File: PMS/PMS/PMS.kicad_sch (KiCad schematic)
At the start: 22 parts

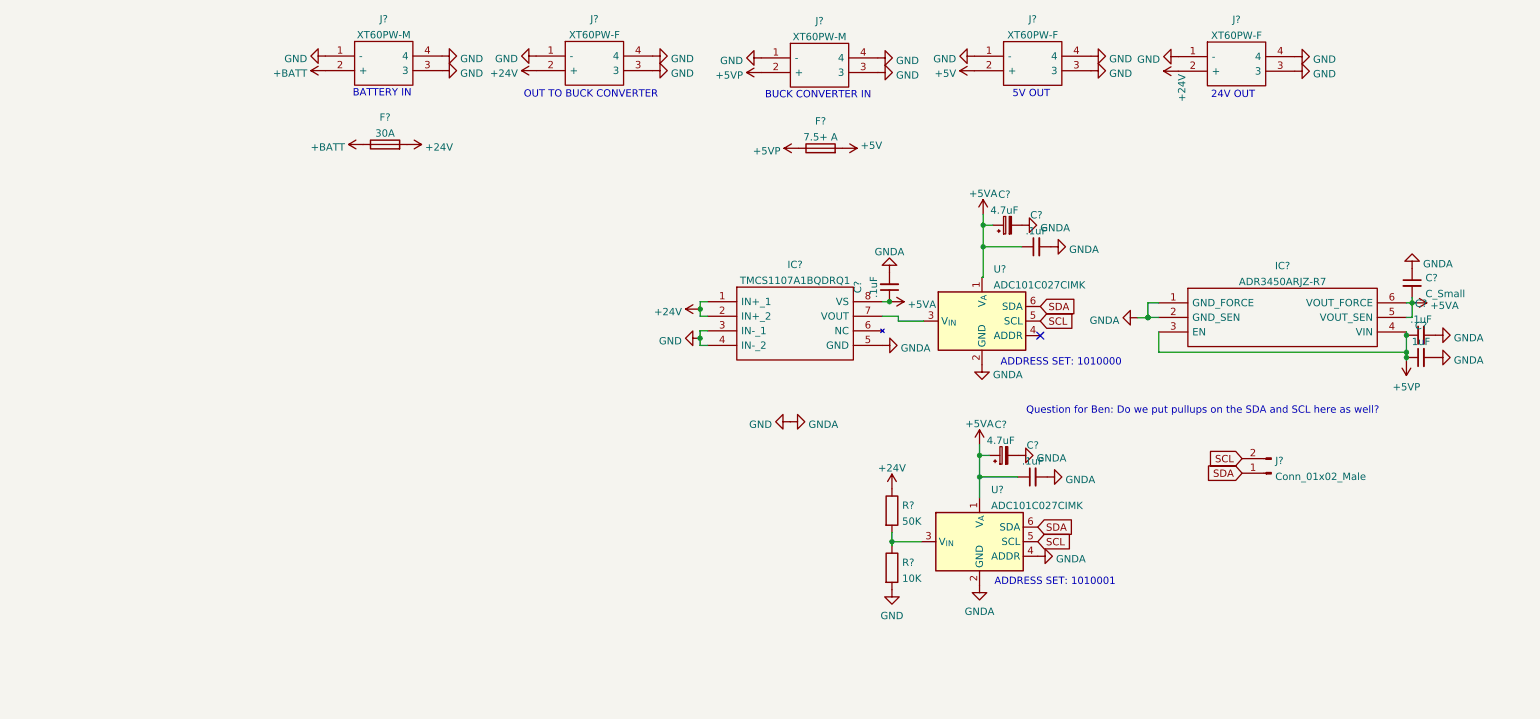
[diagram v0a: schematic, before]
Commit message: several changes to satisfy ERC
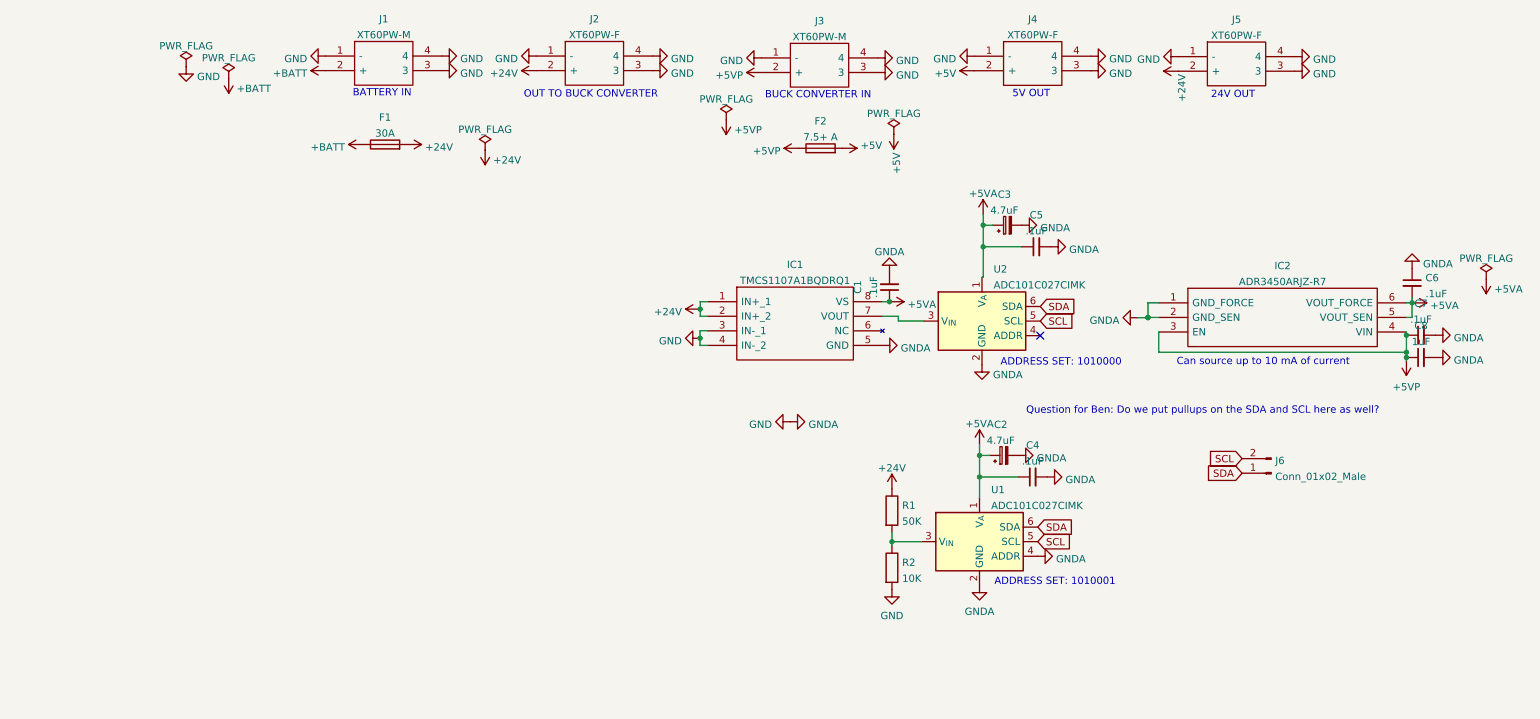
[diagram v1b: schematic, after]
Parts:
- C6: renamed from C?; value C_Small -> .1uF
- IC1: renamed from IC?; footprint SOIC127P600X175-8N -> TMCS1107A1BQDRQ1:SOIC127P600X175-8N
- IC2: renamed from IC?; footprint SOT95P280X145-6N -> ADR3450ARJZ-R7:SOT95P280X145-6N
- J1, J3: renamed from J?; footprint XT60PWM -> LIB_XT60PW-M:XT60PWM
- J2, J4, J5: renamed from J?; footprint XT60PWM -> LIB_XT60PW-F:XT60PWF
- J6: renamed from J?; footprint (none) -> Connector_Molex:Molex_KK-254_AE-6410-02A_1x02_P2.54mm_Vertical
- gave numbers to parts that had none: 13
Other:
- note added: "Can source up to 10 mA of current"

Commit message: Updated PMS. Now includes option for LA12 with other fixes.
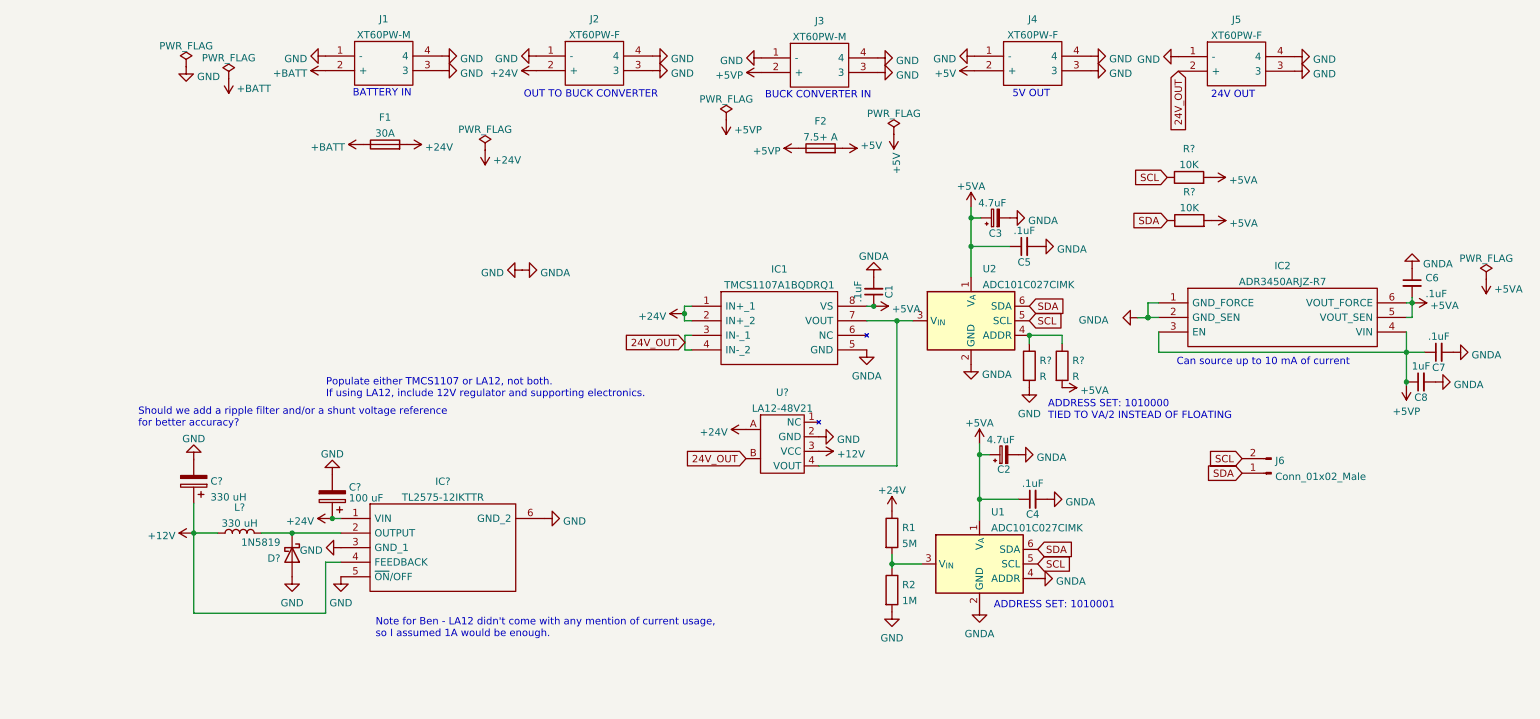
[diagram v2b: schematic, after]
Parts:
- added C?: 330 uH, symbol Device:C_Polarized
- added C?: 100 uF, symbol Device:C_Polarized
- added D?: 1N5819, Diode_THT:D_DO-41_SOD81_P10.16mm_Horizontal, symbol Diode:1N5819
- added IC?: TL2575-12IKTTR, Package_TO_SOT_SMD:TO-263-5_TabPin6, symbol TL2575-12IKTTR:TL2575-12IKTTR
- added L?: 330 uH, symbol Device:L
- added R? (x2): 10K, symbol Device:R
- added R? (x2): R, symbol Device:R
- added U?: LA12-48V21, LA12:LA12-48V21, symbol LA12:LA12-48V21
- R1: value 50K -> 5M
- R2: value 10K -> 1M
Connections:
- net +24V: now also C?.1, IC?.1 (VIN), U?.A; no longer J5.2 (+)
- net +5VA: now also R?.2, R?.2, R?.2
- net GND: now also C?.2, C?.2, D?.2 (A), IC?.3 (GND_1), IC?.5 (~{ON}/OFF), IC?.6 (GND_2), R?.2, U?.2 (GND); no longer IC1.3 (IN-_1), IC1.4 (IN-_2)
- net SCL: now also R?.1
- net SDA: now also R?.1
- net at IC1.7 (VOUT), U2.3 (V_{IN}): now also U?.4 (VOUT)
- net at U2.4 (ADDR): now also R?.1, R?.1
- new net: D?.1 (K), IC?.2 (OUTPUT), L?.2
- new net +12V: C?.1, IC?.4 (FEEDBACK), L?.1, U?.3 (VCC)
- new net 24V_OUT: IC1.3 (IN-_1), IC1.4 (IN-_2), J5.2 (+), U?.B
- no-connect marks 1 -> 0
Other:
- note added: "ADDRESS SET: 1010000 TIED TO VA/2 INSTEAD OF FLOATING"
- note added: "Note for Ben - LA12 didn't come with any mention of current usage, so I assumed 1A would be enough."
- note added: "Populate either TMCS1107 or LA12, not both. If using LA12, include 12V regulator and supporting electronics."
- note added: "Should we add a ripple filter and/or a shunt voltage reference for better accuracy?"
- note removed: "ADDRESS SET: 1010000"
- note removed: "Question for Ben: Do we put pullups on the SDA and SCL here as well?"
- moved on the sheet: C1, C3, C4, C5, C7, C8, IC1, R1, R2, U1, U2

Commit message: annotated schematic
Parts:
- R3, R4: renamed from R?; value R -> 10K
- gave numbers to parts that had none: 8
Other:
- moved on the sheet: R4

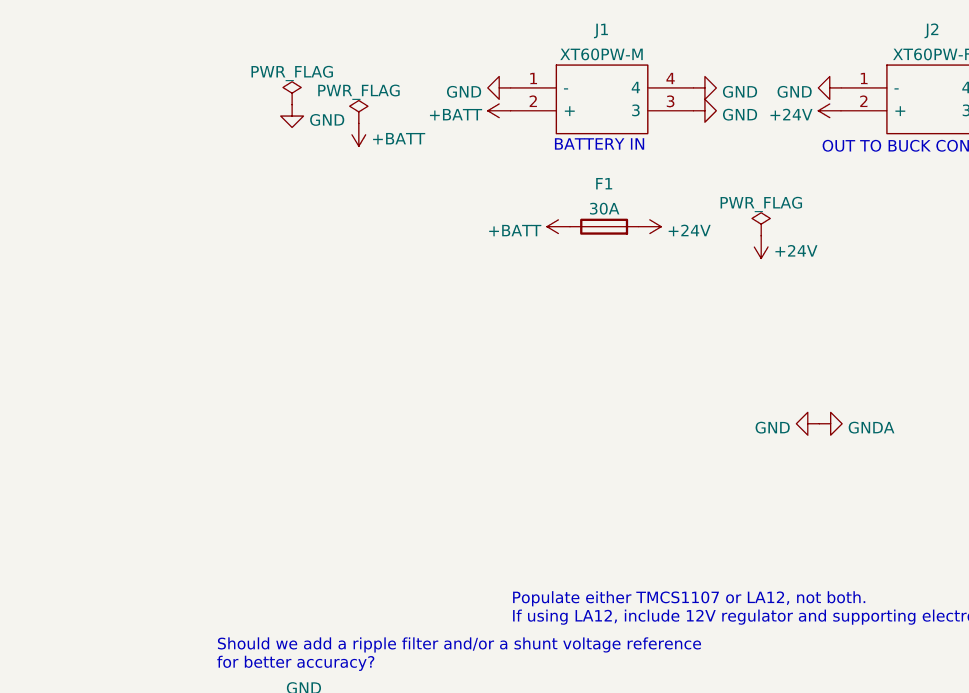
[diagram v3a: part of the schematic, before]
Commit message: added reverse polarity protection
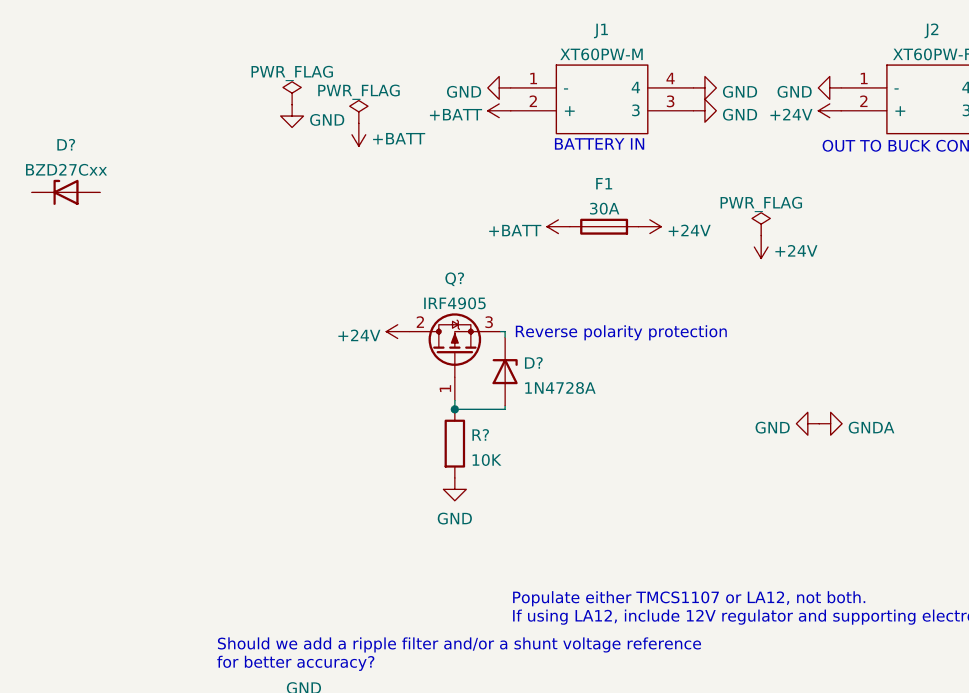
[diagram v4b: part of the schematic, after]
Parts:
- added D?: 1N4728A, Diode_THT:D_DO-41_SOD81_P10.16mm_Horizontal, symbol Diode:1N47xxA
- added D?: BZD27Cxx, Diode_SMD:D_SMF, symbol Diode:BZD27Cxx
- added Q?: IRF4905, Package_TO_SOT_THT:TO-220-3_Vertical, symbol Transistor_FET:IRF4905
- added R?: 10K, symbol Device:R
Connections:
- net +24V: now also Q?.2 (D)
- net GND: now also R?.2
- new net: D?.2 (A), Q?.1 (G), R?.1
- new net: D?.1 (K), Q?.3 (S)
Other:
- note added: "Reverse polarity protection"
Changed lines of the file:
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@@
   (junction (at 242.1128 75.2602) (diameter 0) (color 0 0 0 0)
   )
+  (junction (at 46.482 67.945) (diameter 0) (color 0 0 0 0)
+  )
   (wire (pts (xy 196.0626 77.8002) (xy 196.0626 77.851))
     (stroke (width 0) (type default) (color 0 0 0 0))
@@
     (stroke (width 0) (type default) (color 0 0 0 0))
   )
+  (wire (pts (xy 46.482 67.945) (xy 52.07 67.945))
+    (stroke (width 0) (type default) (color 0 0 0 0))
+  )
   (wire (pts (xy 242.1128 75.2602) (xy 242.1128 77.8002))
     (stroke (width 0) (type default) (color 0 0 0 0))
@@
     (stroke (width 0) (type default) (color 0 0 0 0))
   )
+  (wire (pts (xy 52.07 59.309) (xy 51.562 59.309))
+    (stroke (width 0) (type default) (color 0 0 0 0))
+  )
+  (wire (pts (xy 52.07 67.945) (xy 52.07 67.564))
+    (stroke (width 0) (type default) (color 0 0 0 0))
+  )
   (wire (pts (xy 166.7002 109.4994) (xy 173.4312 109.4994))
     (stroke (width 0) (type default) (color 0 0 0 0))
@@
     (stroke (width 0) (type default) (color 0 0 0 0))
   )
+  (wire (pts (xy 46.482 66.929) (xy 46.482 67.945))
+    (stroke (width 0) (type default) (color 0 0 0 0))
+  )
   (wire (pts (xy 152.2984 78.3844) (xy 155.067 78.3844))
     (stroke (width 0) (type default) (color 0 0 0 0))
@@
   )
   (wire (pts (xy 197.9422 83.8708) (xy 241.1222 83.8708))
+    (stroke (width 0) (type default) (color 0 0 0 0))
+  )
+  (wire (pts (xy 52.07 59.944) (xy 52.07 59.309))
     (stroke (width 0) (type default) (color 0 0 0 0))
   )
@@
   )
   (text "24V OUT" (at 207.0608 39.7764 0)
+    (effects (font (size 1.27 1.27)) (justify left bottom))
+  )
+  (text "Reverse polarity protection" (at 53.086 60.325 0)
     (effects (font (size 1.27 1.27)) (justify left bottom))
   )
@@
     (pin "1")
   )
+  (symbol (lib_id "Device:R") (at 46.482 71.755 0) (unit 1)
+    (in_bom yes) (on_board yes) (fields_autoplaced)
+    (property "Reference" "R?" (id 0) (at 48.26 70.8465 0)
+      (effects (font (size 1.27 1.27)) (justify left))
+    )
+    (property "Value" "10K" (id 1) (at 48.26 73.6216 0)
+      (effects (font (size 1.27 1.27)) (justify left))
+    )
+    (property "Footprint" "" (id 2) (at 44.704 71.755 90)
+      (effects (font (size 1.27 1.27)) hide)
+    )
+    (property "Datasheet" "~" (id 3) (at 46.482 71.755 0)
+      (effects (font (size 1.27 1.27)) hide)
+    )
+    (pin "1")
+    (pin "2")
+  )
   (symbol (lib_id "power:GNDA") (at 173.482 101.727 90) (unit 1)
     (in_bom yes) (on_board yes) (fields_autoplaced)
@@
     (pin "1")
   )
+  (symbol (lib_id "Diode:1N47xxA") (at 52.07 63.754 270) (unit 1)
+    (in_bom yes) (on_board yes) (fields_autoplaced)
+    (property "Reference" "D?" (id 0) (at 54.102 62.8455 90)
+      (effects (font (size 1.27 1.27)) (justify left))
+    )
+    (property "Value" "1N4728A" (id 1) (at 54.102 65.6206 90)
+      (effects (font (size 1.27 1.27)) (justify left))
+    )
+    (property "Footprint" "Diode_THT:D_DO-41_SOD81_P10.16mm_Horizontal" (id 2) (at 47.625 63.754 0)
+      (effects (font (size 1.27 1.27)) hide)
+    )
+    (property "Datasheet" "https://www.vishay.com/docs/85816/1n4728a.pdf" (id 3) (at 52.07 63.754 0)
+      (effects (font (size 1.27 1.27)) hide)
+    )
+    (pin "1")
+    (pin "2")
+  )
+  (symbol (lib_id "Transistor_FET:IRF4905") (at 46.482 61.849 90) (unit 1)
+    (in_bom yes) (on_board yes) (fields_autoplaced)
+    (property "Reference" "Q?" (id 0) (at 46.482 53.4375 90))
+    (property "Value" "IRF4905" (id 1) (at 46.482 56.2126 90))
+    (property "Footprint" "Package_TO_SOT_THT:TO-220-3_Vertical" (id 2) (at 48.387 56.769 0)
+      (effects (font (size 1.27 1.27) italic) (justify left) hide)
+    )
+    (property "Datasheet" "http://www.infineon.com/dgdl/irf4905.pdf?fileId=5546d462533600a4015355e32165197c" (id 3) (at 46.482 61.849 0)
+      (effects (font (size 1.27 1.27)) (justify left) hide)
+    )
+    (pin "1")
+    (pin "2")
+    (pin "3")
+  )
   (symbol (lib_id "XT60PW-M:XT60PW-M") (at 128.651 32.5628 0) (unit 1)
     (in_bom yes) (on_board yes) (fields_autoplaced)
@@
     (pin "2")
   )
+  (symbol (lib_id "Diode:BZD27Cxx") (at 3.2766 43.8404 0) (unit 1)
+    (in_bom yes) (on_board yes) (fields_autoplaced)
+    (property "Reference" "D?" (id 0) (at 3.2766 38.6039 0))
+    (property "Value" "BZD27Cxx" (id 1) (at 3.2766 41.379 0))
+    (property "Footprint" "Diode_SMD:D_SMF" (id 2) (at 3.2766 48.2854 0)
+      (effects (font (size 1.27 1.27)) hide)
+    )
+    (property "Datasheet" "https://www.vishay.com/docs/85153/bzd27series.pdf" (id 3) (at 3.2766 43.8404 0)
+      (effects (font (size 1.27 1.27)) hide)
+    )
+    (pin "1")
+    (pin "2")
+  )
+  (symbol (lib_id "power:GND") (at 46.482 75.565 0) (unit 1)
+    (in_bom yes) (on_board yes) (fields_autoplaced)
+    (property "Reference" "#PWR?" (id 0) (at 46.482 81.915 0)
+      (effects (font (size 1.27 1.27)) hide)
+    )
+    (property "Value" "GND" (id 1) (at 46.482 80.1275 0))
+    (property "Footprint" "" (id 2) (at 46.482 75.565 0)
+      (effects (font (size 1.27 1.27)) hide)
+    )
+    (property "Datasheet" "" (id 3) (at 46.482 75.565 0)
+      (effects (font (size 1.27 1.27)) hide)
+    )
+    (pin "1")
+  )
   (symbol (lib_id "power:GNDA") (at 194.2592 77.851 270) (unit 1)
     (in_bom yes) (on_board yes)
@@
     (pin "1")
   )
+  (symbol (lib_id "power:+24V") (at 41.402 59.309 90) (unit 1)
+    (in_bom yes) (on_board yes) (fields_autoplaced)
+    (property "Reference" "#PWR?" (id 0) (at 45.212 59.309 0)
+      (effects (font (size 1.27 1.27)) hide)
+    )
+    (property "Value" "+24V" (id 1) (at 38.227 59.788 90)
+      (effects (font (size 1.27 1.27)) (justify left))
+    )
+    (property "Footprint" "" (id 2) (at 41.402 59.309 0)
+      (effects (font (size 1.27 1.27)) hide)
+    )
+    (property "Datasheet" "" (id 3) (at 41.402 59.309 0)
+      (effects (font (size 1.27 1.27)) hide)
+    )
+    (pin "1")
+  )
   (symbol (lib_id "power:PWR_FLAG") (at 35.814 36.1696 0) (unit 1)
     (in_bom yes) (on_board yes) (fields_autoplaced)
@@
       (reference "#PWR067") (unit 1) (value "+5VA") (footprint "")
     )
+    (path "/a0be2698-ea96-4daa-a18d-7ebc3407a696"
+      (reference "#PWR?") (unit 1) (value "GND") (footprint "")
+    )
+    (path "/d5bebcb2-5427-41be-82cc-5e6f9a078f45"
+      (reference "#PWR?") (unit 1) (value "+24V") (footprint "")
+    )
     (path "/22897773-dfc2-443a-8445-c71410d2ee57"
       (reference "C1") (unit 1) (value ".1uF") (footprint "")
@@
       (reference "D1") (unit 1) (value "1N5819") (footprint "Diode_THT:D_DO-41_SOD81_P10.16mm_Horizontal")
     )
+    (path "/8c58b9c6-42fa-43ad-a456-e387b2c947c3"
+      (reference "D?") (unit 1) (value "1N4728A") (footprint "Diode_THT:D_DO-41_SOD81_P10.16mm_Horizontal")
+    )
+    (path "/9cf62153-2e7b-4838-ba92-d00a36e9a345"
+      (reference "D?") (unit 1) (value "BZD27Cxx") (footprint "Diode_SMD:D_SMF")
+    )
     (path "/f7d7bb3d-3174-4f8d-bddb-cbcecab3f605"
       (reference "F1") (unit 1) (value "30A") (footprint "")
@@
       (reference "L1") (unit 1) (value "330 uH") (footprint "")
     )
+    (path "/9259a944-3fbe-4710-912e-c818d1125aa8"
+      (reference "Q?") (unit 1) (value "IRF4905") (footprint "Package_TO_SOT_THT:TO-220-3_Vertical")
+    )
     (path "/45100c78-fff6-4f44-a47d-2aea8091517a"
       (reference "R1") (unit 1) (value "5M") (footprint "")
@@
       (reference "R6") (unit 1) (value "10K") (footprint "")
     )
+    (path "/33d1fa0e-96de-4bd9-8bed-eb3d75d0d7d8"
+      (reference "R?") (unit 1) (value "10K") (footprint "")
+    )
     (path "/f3cbf47b-61db-48c0-a21c-fc2a80beb037"
